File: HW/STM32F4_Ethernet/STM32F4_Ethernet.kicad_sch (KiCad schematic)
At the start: 0 parts

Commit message: Progress backup
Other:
- added sheet Power (power.kicad_sch)
- added sheet USB (USB.kicad_sch)

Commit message: Progress backup. add SRAM
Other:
- sheet Ethernet ports: added CLK_25Mhz, MII_COL, MII_CRS, MII_RXD0, MII_RXD1, MII_RXD2, MII_RXD3, MII_RX_CLK, MII_RX_DV, MII_TXD0, MII_TXD1, MII_TXD2, MII_TXD3, MII_TX_CLK, MII_TX_EN, PHY_SPI_CLK, PHY_SPI_CS, PHY_SPI_MISO, PHY_SPI_MOSI, ~{MII_INTRN}, ~{PHY_RESET}; removed none

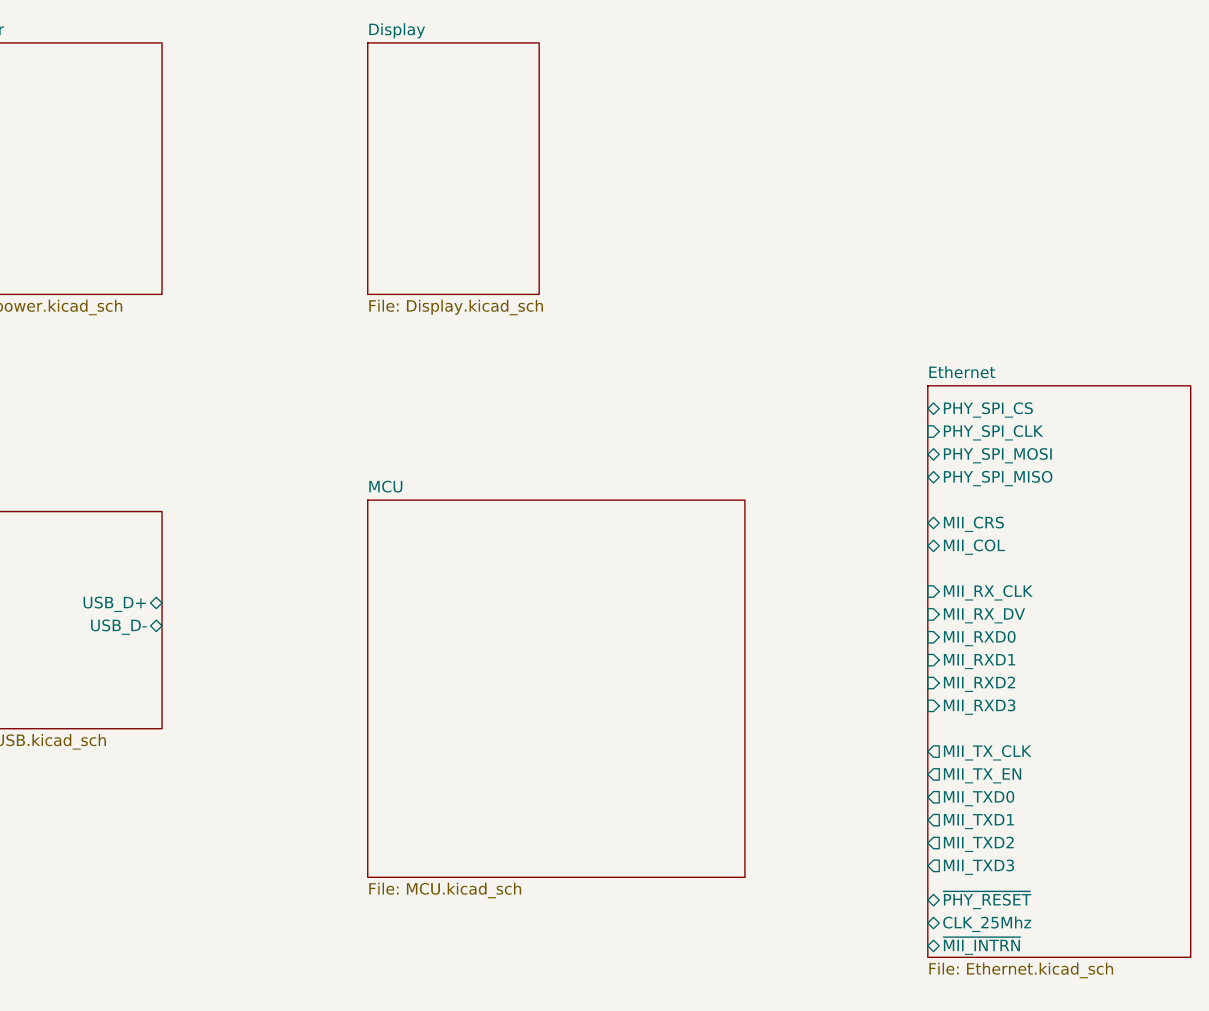
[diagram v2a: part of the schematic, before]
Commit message: Sample PCB. Need to update RLC Size
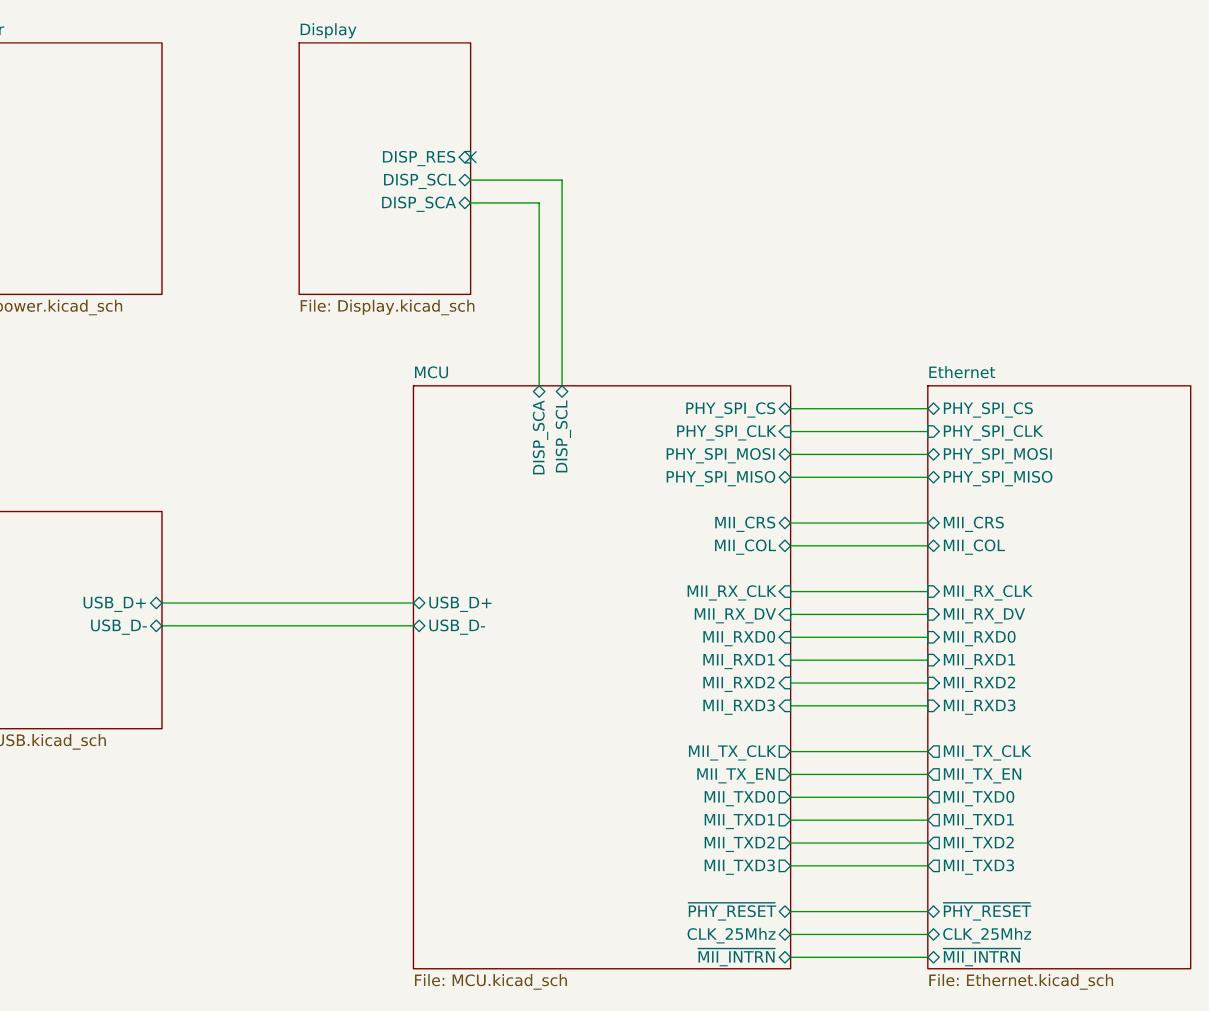
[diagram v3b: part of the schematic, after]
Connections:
- no-connect marks 0 -> 1
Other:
- sheet Display ports: added DISP_RES, DISP_SCA, DISP_SCL; removed none
- sheet MCU ports: added CLK_25Mhz, DISP_SCA, DISP_SCL, MII_COL, MII_CRS, MII_RXD0, MII_RXD1, MII_RXD2, MII_RXD3, MII_RX_CLK, MII_RX_DV, MII_TXD0, MII_TXD1, MII_TXD2, MII_TXD3, MII_TX_CLK, MII_TX_EN, PHY_SPI_CLK, PHY_SPI_CS, PHY_SPI_MISO, PHY_SPI_MOSI, USB_D+, USB_D-, ~{MII_INTRN}, ~{PHY_RESET}; removed none
